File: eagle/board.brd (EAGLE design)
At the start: 115.2 x 49.5 mm, 26 parts, among them Q1 5MHz, U1 P8X32A-D40, U2 74LS138N, U3 74LS139N, U4 24C256

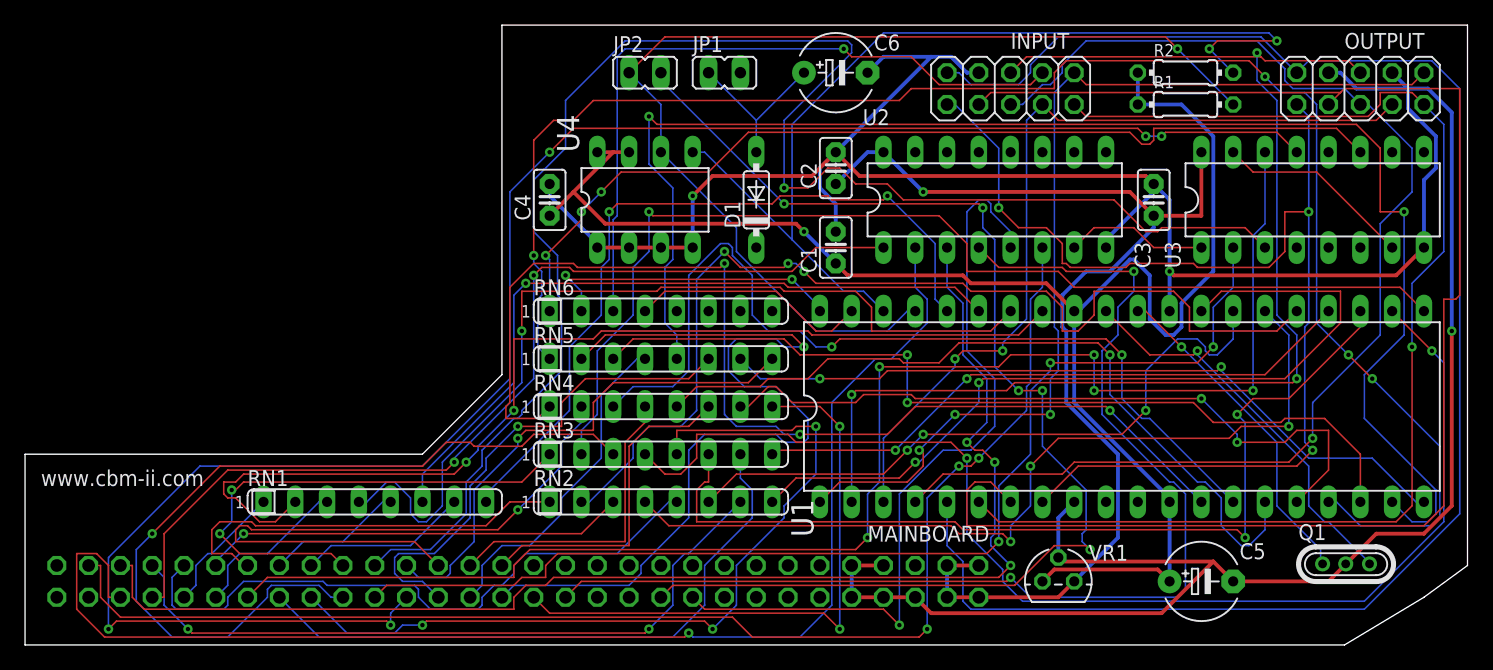
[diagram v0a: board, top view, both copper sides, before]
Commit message: Board and firmware fixes.
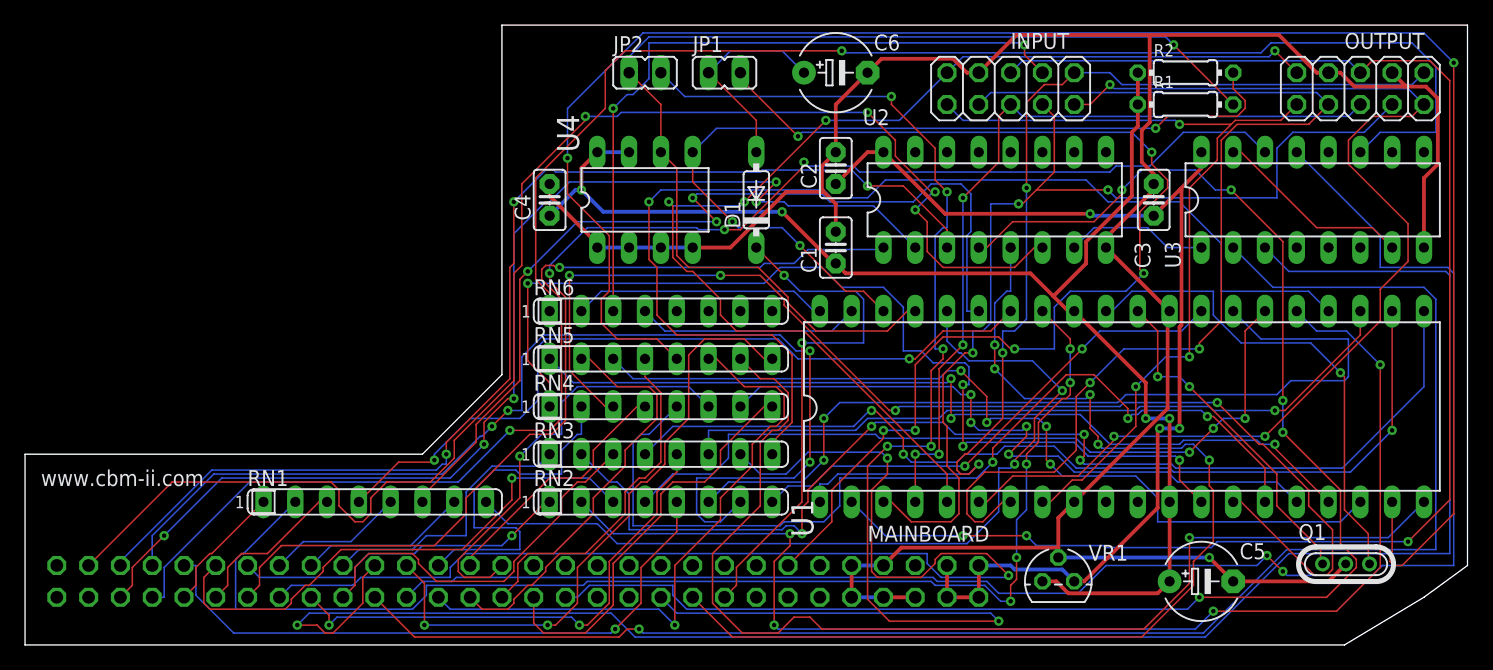
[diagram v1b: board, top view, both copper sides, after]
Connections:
- net /EXTRES: now also MAINBOARD.14
- net /RES: now also MAINBOARD.17
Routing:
- net /EXTRES: track 0.00 -> 93.2 mm, vias 0 -> 6
- net N$19: track 132.7 -> 69.8 mm, vias 4 -> 3
- net GND: track 258.7 -> 204.0 mm, vias 3 -> 1
- net A3: track 50.4 -> 97.2 mm, vias 0 -> 2
- net N$12: track 49.2 -> 92.1 mm, vias 2 -> 1
- net /RES: track 0.00 -> 41.6 mm, vias 0 -> 2
- net D4: track 70.7 -> 29.7 mm, vias 1 -> 0
- net B1: track 131.3 -> 92.8 mm, vias 0 -> 4
- net A14: track 90.4 -> 127.1 mm, vias 3 -> 1
- net A1: track 67.1 -> 30.4 mm, vias 1 -> 0
- net G0: track 99.0 -> 64.8 mm, vias 1 -> 4
- net A7: track 56.7 -> 90.3 mm, vias 2 -> 4
- net R1: track 120.7 -> 87.9 mm, vias 0 -> 2
- net PHI1: track 93.7 -> 124.1 mm, vias 2 -> 5
- net N$16: track 60.3 -> 89.6 mm, vias 2 -> 1
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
